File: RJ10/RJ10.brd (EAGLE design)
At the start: 20 x 35 mm, 2 parts, among them J1 SS-641010-NF

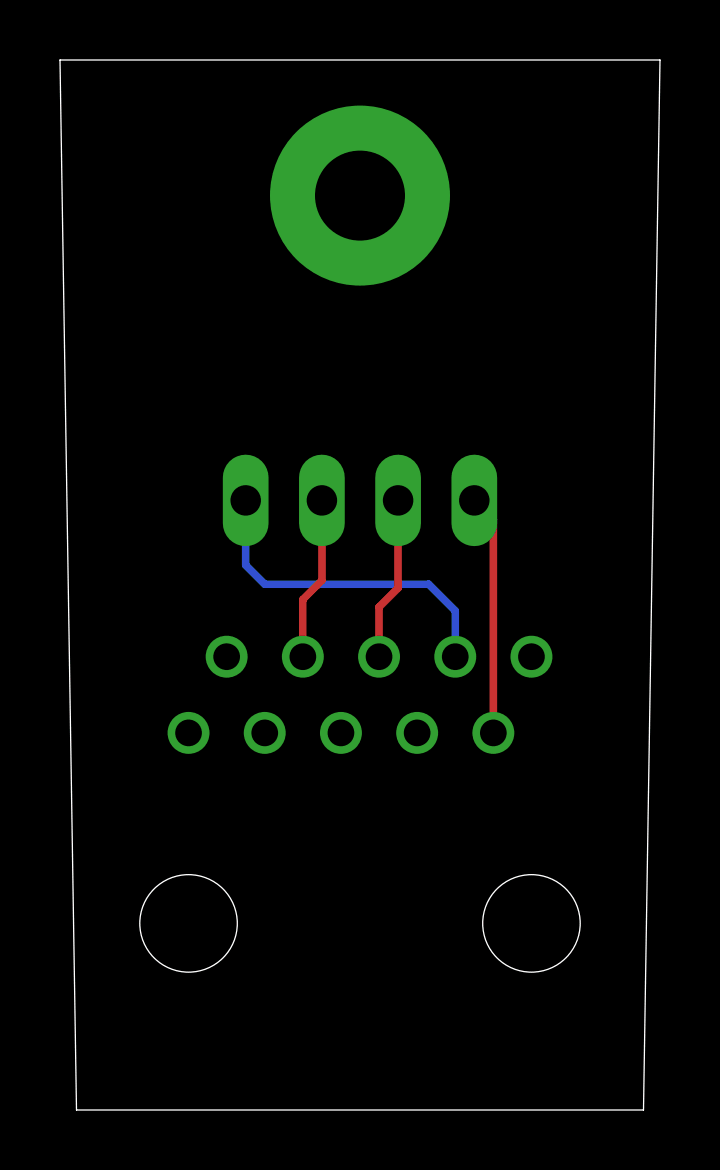
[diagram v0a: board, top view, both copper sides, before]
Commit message: Added silkscreen texts
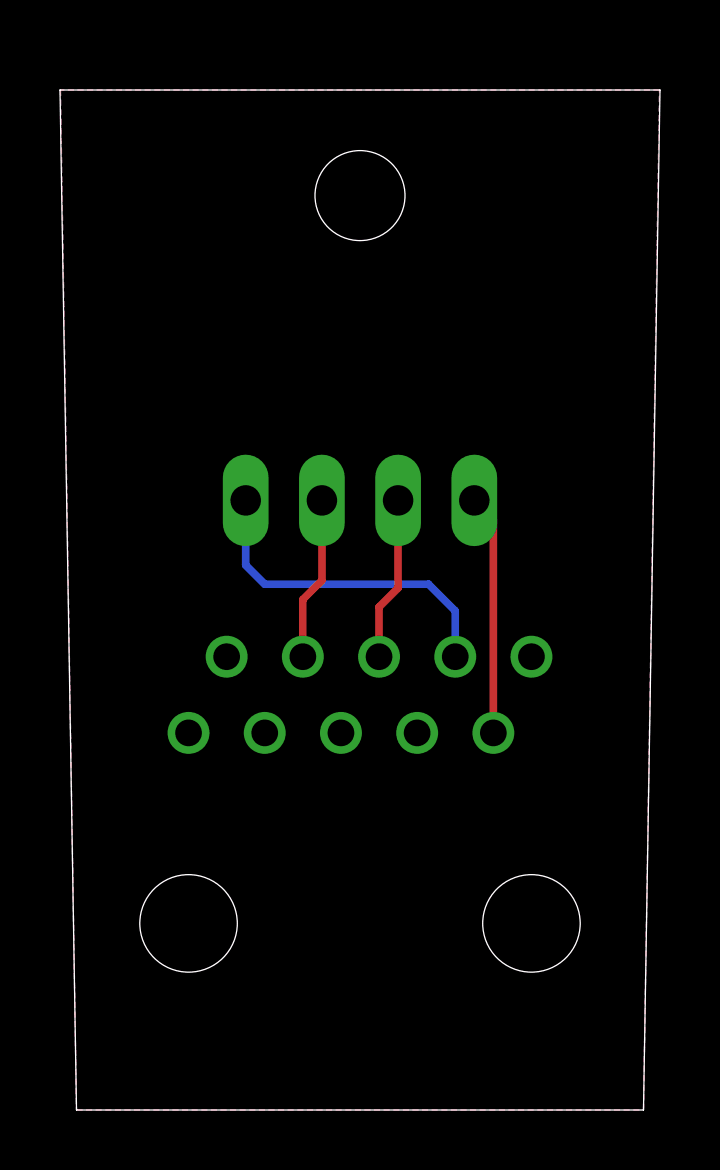
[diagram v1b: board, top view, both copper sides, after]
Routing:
- added copper zone on layer 1, net GND
- added copper zone on layer 16, net GND
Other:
- board size 20 x 35 mm -> 20 x 34 mm
- board text added: "VUSB RD D- WH D+ GN GND BK"
